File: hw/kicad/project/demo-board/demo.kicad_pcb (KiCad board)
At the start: 2 copper layers, 49.5 x 49.5 mm, 28 parts, among them J2 MICRO_SD_HINGE, P1 ESP_CONN, P2 ESP_CONN, P3 ESP_CONN, P4 PWR_CONN, P5 CONN_DISPLAY, P6 SD_LCD_CONN, SW1 KEY_FLASH, SW2 KEY_RST, U1 NCP1117ST33T3G, U2 ESP-12E

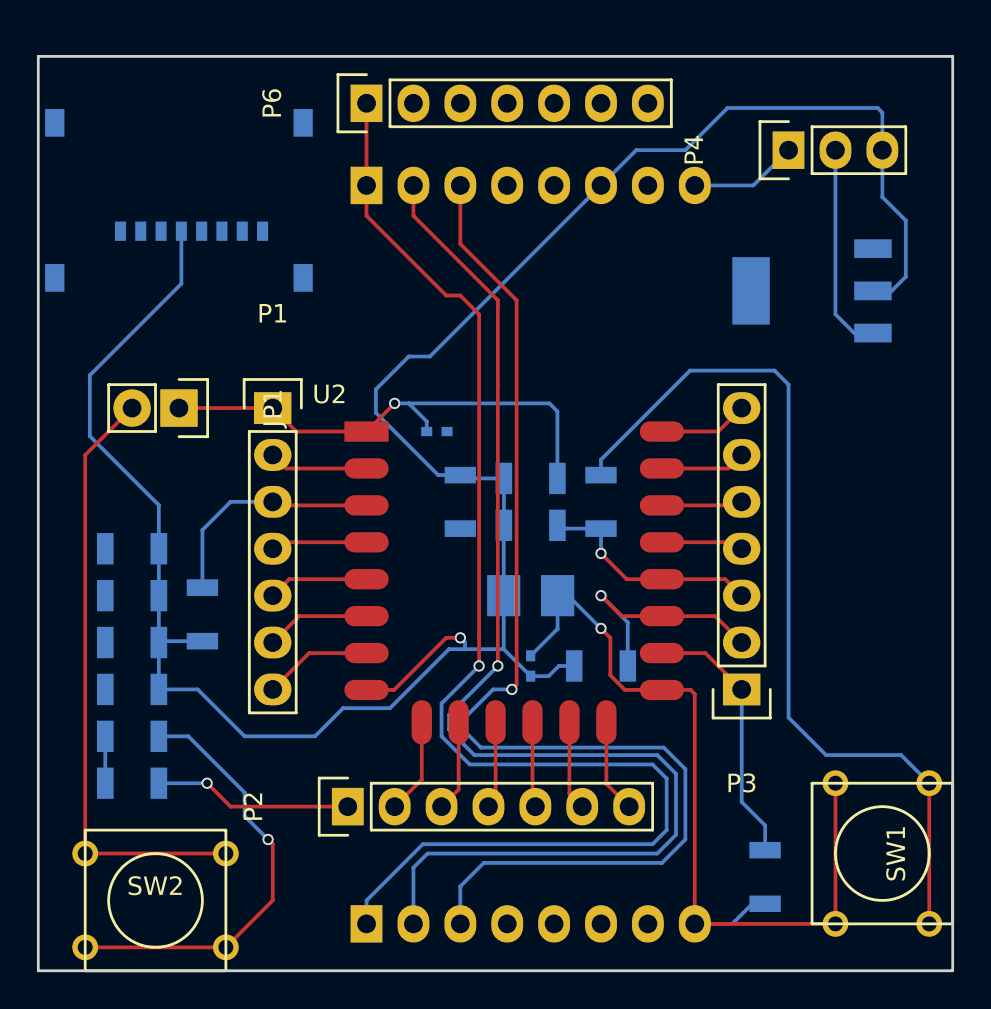
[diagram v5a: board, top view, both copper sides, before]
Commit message: Board routing completed
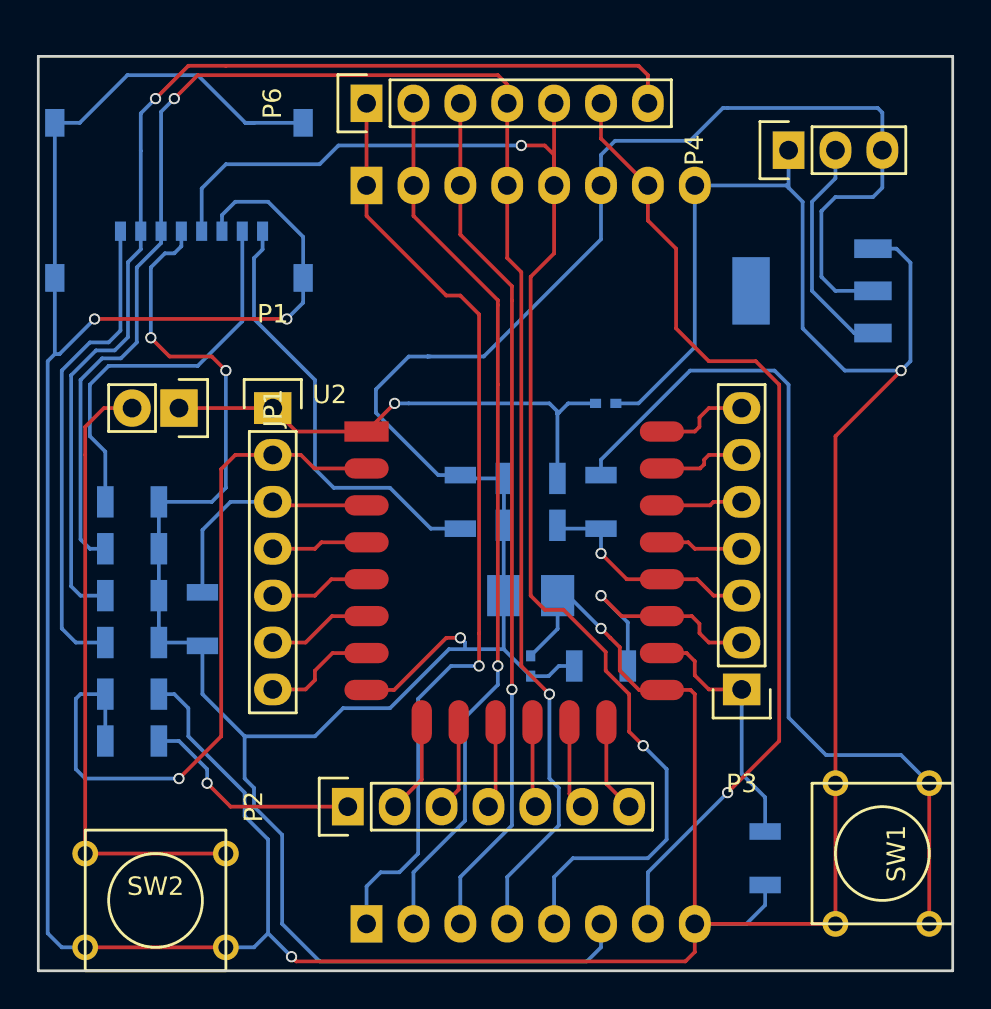
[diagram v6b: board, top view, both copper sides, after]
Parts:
- moved C2 9.27 mm to (153.9, 88.6)
- moved R13 7.62 mm to (128.3, 96.5)
- moved R12 5.08 mm to (128.3, 94.0)
- moved R15 5.08 mm to (128.3, 101.6)
- moved R14 2.54 mm to (128.3, 99.1)
- moved R2 2.29 mm to (128.3, 106.9)
- moved R3 2.29 mm to (128.3, 104.4)
- moved R10 1.02 mm to (162.6, 113.3)
- moved R8 0.25 mm to (132.1, 100.3)
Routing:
- net GND: track 76.1 -> 253.7 mm, vias 2 -> 5
- net /SD_LCD_MOSI: track 0.00 -> 94.7 mm, vias 0 -> 2
- net /SD_LCD_CLK: track 0.00 -> 76.6 mm, vias 0 -> 2
- net /SD_CS: track 0.00 -> 60.1 mm, vias 0 -> 1
- net /LCD_LED: track 0.00 -> 52.9 mm, vias 0 -> 1
- net VCC: track 128.4 -> 166.2 mm, vias 1 -> 3
- net /ADC: track 7.92 -> 40.1 mm, vias 0 -> 1
- net Net-(J2-Pad1): track 0.00 -> 26.1 mm
- net Net-(J2-Pad8): track 0.00 -> 23.7 mm
- net /LCD_RST: track 73.1 -> 51.4 mm
- net /SD_LCD_MISO: track 0.00 -> 21.3 mm
- net /LCD_CS: track 67.1 -> 48.2 mm
- net /SD_LCD_DATA_CMD: track 64.5 -> 46.8 mm
- net /ADC_EX: track 10.8 -> 12.2 mm
- net 5V: track 11.3 -> 12.4 mm
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
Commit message: Net classes clarified
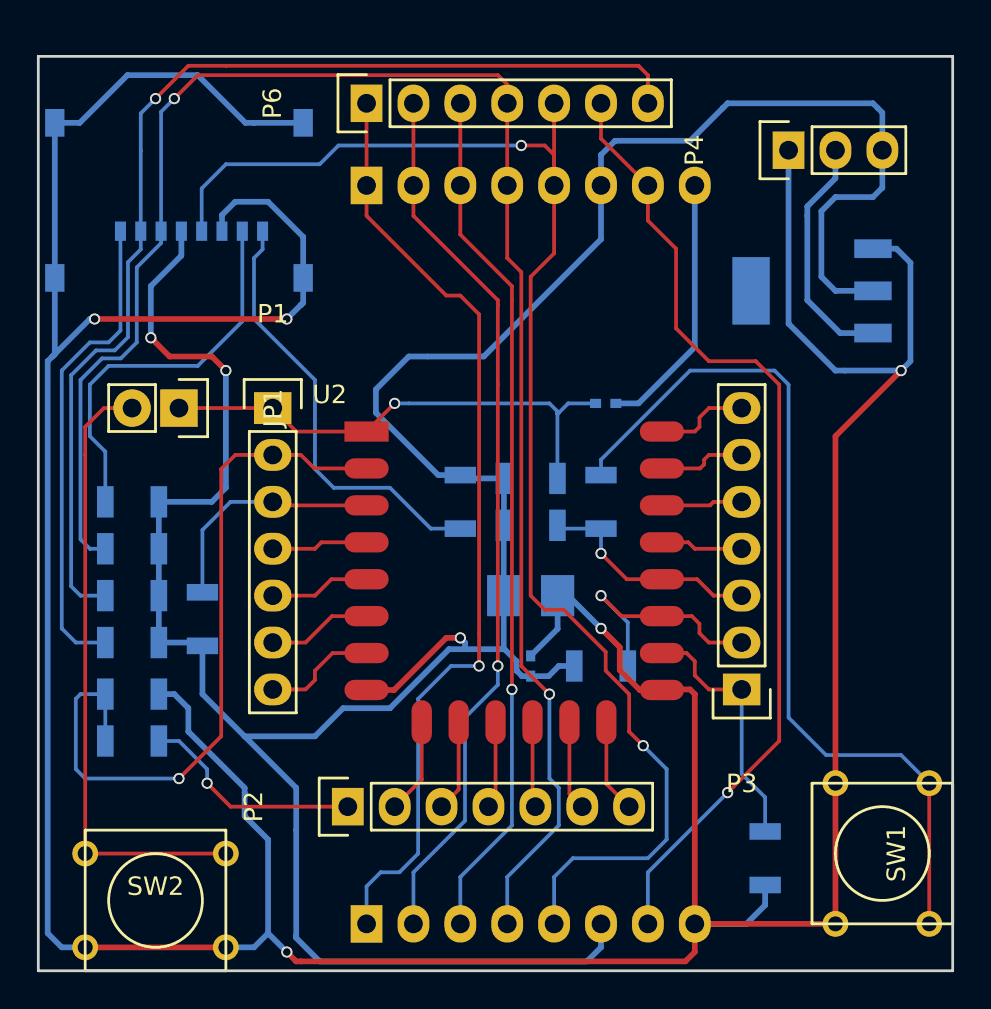
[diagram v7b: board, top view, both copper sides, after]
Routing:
- net GND: track 253.7 -> 250.5 mm
- net 5V: track 12.4 -> 14.1 mm
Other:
- net class Itead power added: clearance 0.31, trace_width 0.31, via_dia 0.61, via_drill 0.41

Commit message: Added power planes
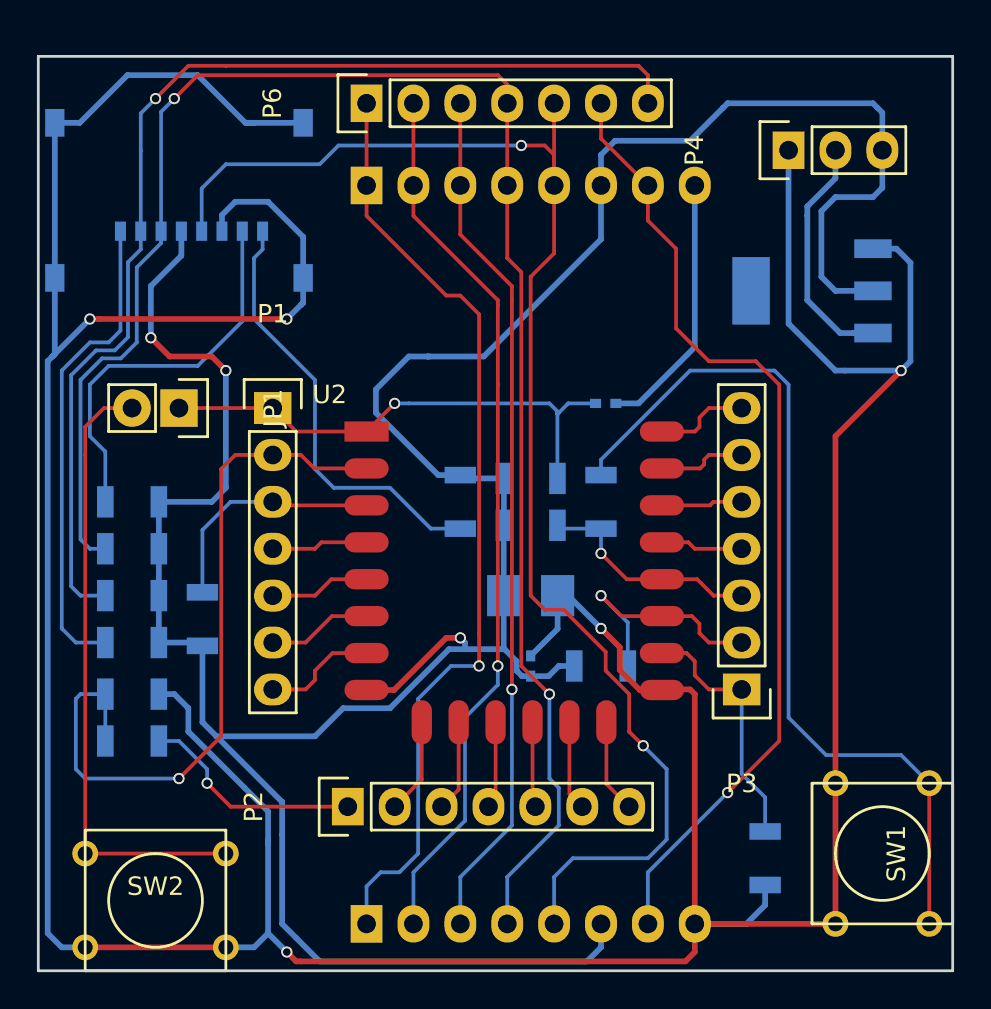
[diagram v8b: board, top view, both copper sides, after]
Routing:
- net VCC: track 166.5 -> 168.0 mm
- added copper zone on B.Cu, net GND
- added copper zone on F.Cu, net GND
